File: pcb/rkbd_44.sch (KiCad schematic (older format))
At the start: 16 parts, among them SW1 SW_Push, U1 ATmega32U4-AU, Y1 16MHz

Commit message: pcb new
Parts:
- R1, R2, R3, R4: footprint Keebio-Parts:R_0805 -> Resistor_SMD:R_0805_2012Metric
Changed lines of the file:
@@
 F 0 "R4" V 4229 3390 50  0000 C CNN
 F 1 "10k" V 4320 3390 50  0000 C CNN
-F 2 "Keebio-Parts:R_0805" H 4425 3390 50  0001 C CNN
+F 2 "Resistor_SMD:R_0805_2012Metric" H 4425 3390 50  0001 C CNN
 F 3 "~" H 4425 3390 50  0001 C CNN
 	1    4425 3390
@@
 F 0 "R2" V 2299 2290 50  0000 C CNN
 F 1 "22" V 2390 2290 50  0000 C CNN
-F 2 "Keebio-Parts:R_0805" H 2495 2290 50  0001 C CNN
+F 2 "Resistor_SMD:R_0805_2012Metric" H 2495 2290 50  0001 C CNN
 F 3 "~" H 2495 2290 50  0001 C CNN
 	1    2495 2290
@@
 F 0 "R3" V 1994 2390 50  0000 C CNN
 F 1 "22" V 2085 2390 50  0000 C CNN
-F 2 "Keebio-Parts:R_0805" H 2190 2390 50  0001 C CNN
+F 2 "Resistor_SMD:R_0805_2012Metric" H 2190 2390 50  0001 C CNN
 F 3 "~" H 2190 2390 50  0001 C CNN
 	1    2190 2390
@@
 F 0 "R1" H 2686 1094 50  0000 R CNN
 F 1 "10k" H 2686 1185 50  0000 R CNN
-F 2 "Keebio-Parts:R_0805" H 2745 1140 50  0001 C CNN
+F 2 "Resistor_SMD:R_0805_2012Metric" H 2745 1140 50  0001 C CNN
 F 3 "~" H 2745 1140 50  0001 C CNN
 	1    2745 1140

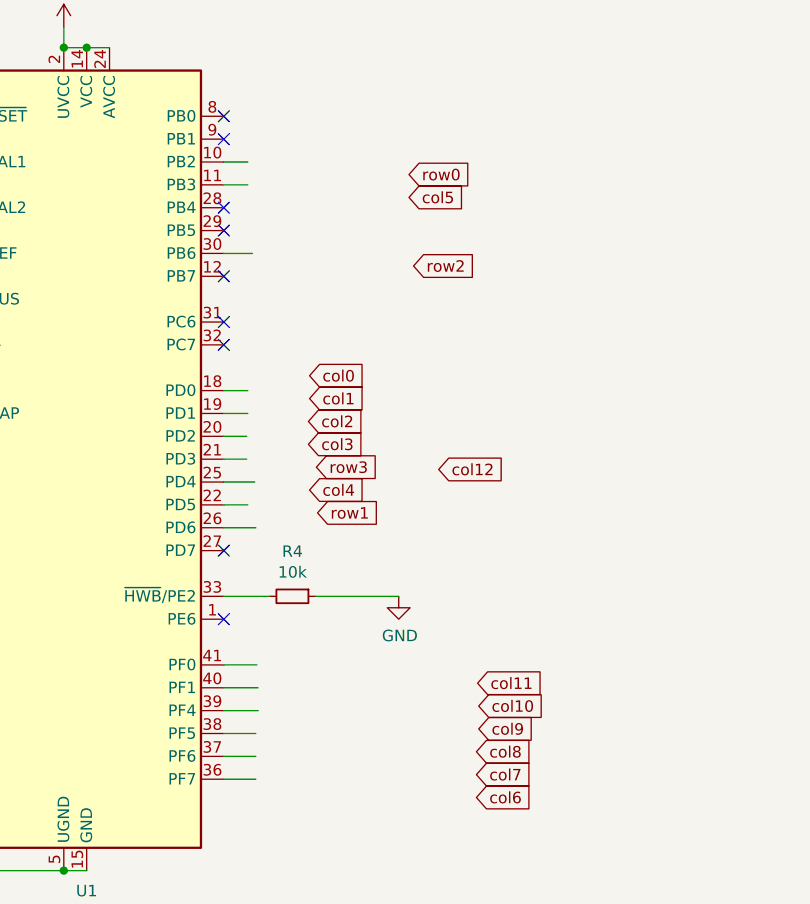
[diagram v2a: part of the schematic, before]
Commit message: add cutting line
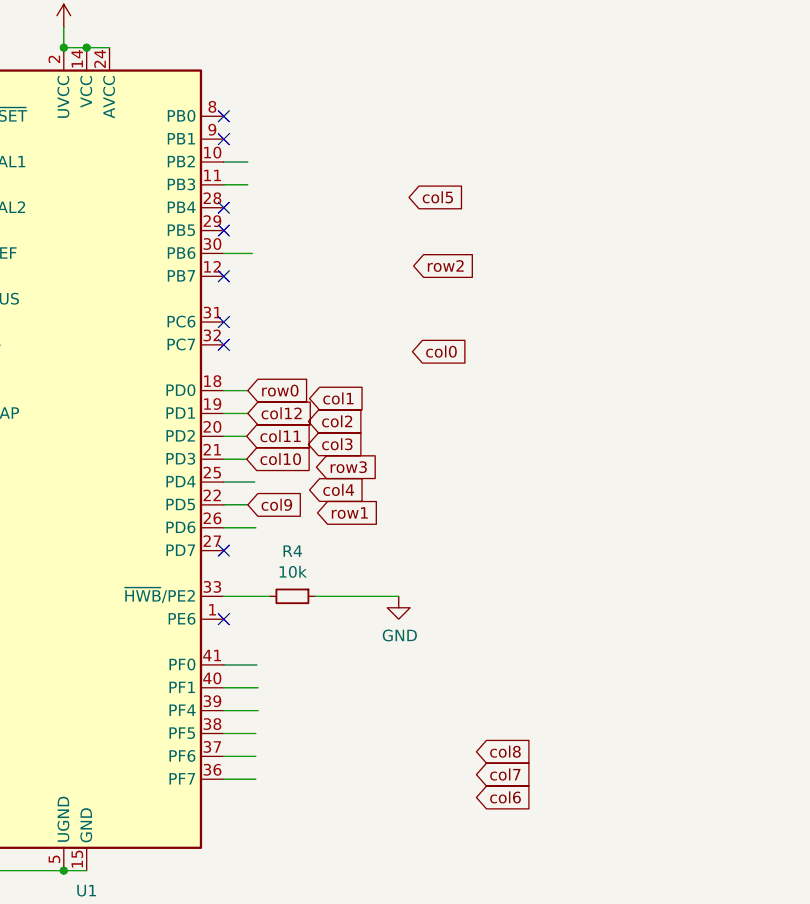
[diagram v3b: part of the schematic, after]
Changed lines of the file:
@@
 Text GLabel 5230 4070 2    50   Input ~ 0
 col8
-Text GLabel 5240 3970 2    50   Input ~ 0
+Text GLabel 4230 2990 2    50   Input ~ 0
 col9
-Text GLabel 5240 3870 2    50   Input ~ 0
+Text GLabel 4225 2790 2    50   Input ~ 0
 col10
 Text GLabel 4530 2825 2    50   Input ~ 0
@@
 Text GLabel 4955 1945 2    50   Input ~ 0
 row2
-Text GLabel 4935 1545 2    50   Input ~ 0
+Text GLabel 4230 2490 2    50   Input ~ 0
 row0
 Wire Wire Line
@@
 Wire Wire Line
 	4265 3090 4125 3090
-Text GLabel 5235 3770 2    50   Input ~ 0
+Text GLabel 4225 2690 2    50   Input ~ 0
 col11
 Text GLabel 4500 2525 2    50   Input ~ 0
 col1
-Text GLabel 4500 2425 2    50   Input ~ 0
+Text GLabel 4950 2320 2    50   Input ~ 0
 col0
 Text GLabel 4535 3025 2    50   Input ~ 0
@@
 Wire Wire Line
 	1970 1290 2060 1290
-Text GLabel 5065 2835 2    50   Input ~ 0
+Text GLabel 4230 2590 2    50   Input ~ 0
 col12
 Connection ~ 3425 4590

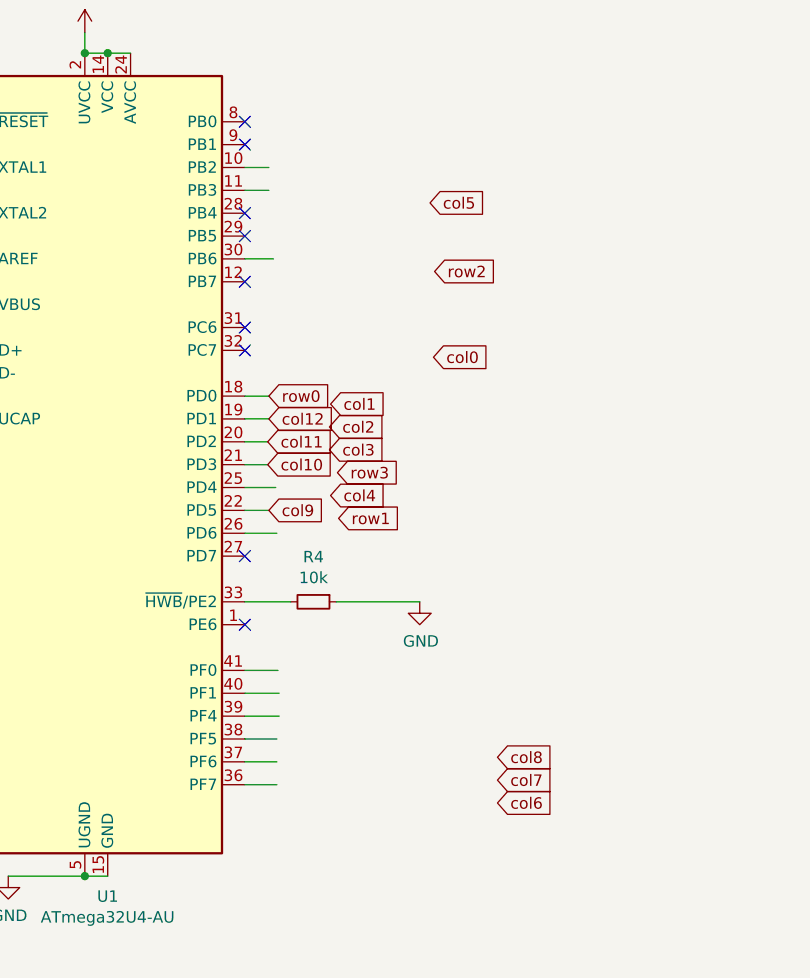
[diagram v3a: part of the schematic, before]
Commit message: Routing all, Ground fills
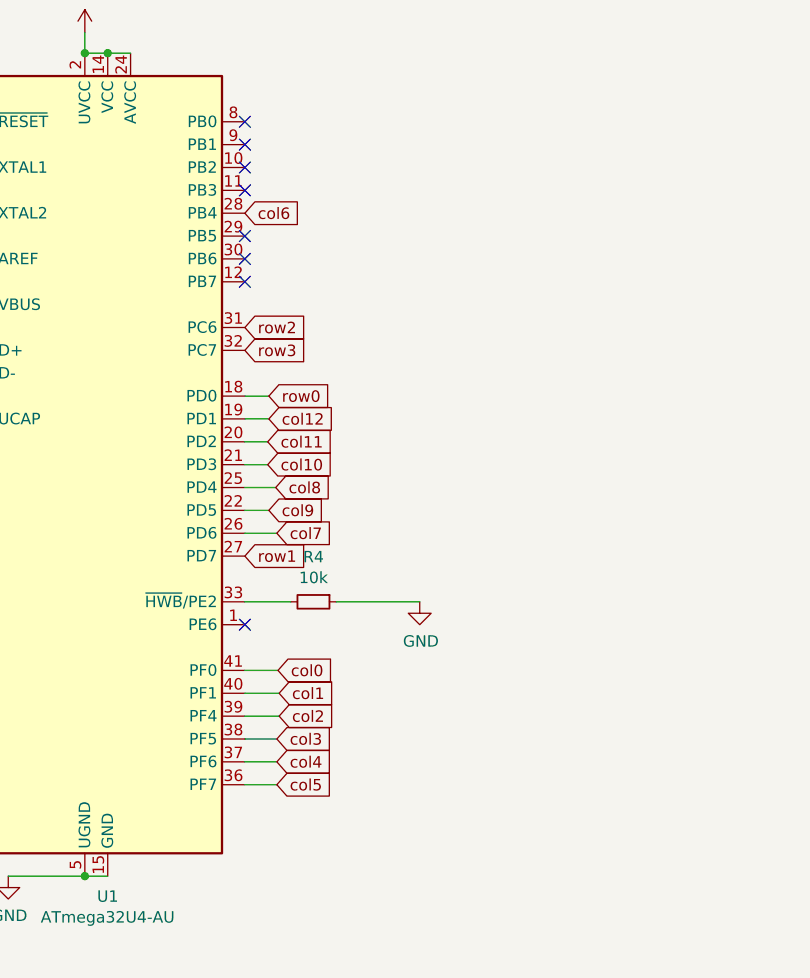
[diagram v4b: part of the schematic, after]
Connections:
- wire segments 69 -> 66
- no-connect marks 12 -> 11
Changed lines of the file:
@@
 F1 "matrix.sch" 50
 $EndSheet
-Text GLabel 4495 2725 2    50   Input ~ 0
+Text GLabel 4265 3990 2    50   Input ~ 0
 col3
-Text GLabel 4500 2925 2    50   Input ~ 0
+Text GLabel 4265 4090 2    50   Input ~ 0
 col4
-Text GLabel 4935 1645 2    50   Input ~ 0
+Text GLabel 4265 4190 2    50   Input ~ 0
 col5
-Text GLabel 5230 4270 2    50   Input ~ 0
+Text GLabel 4125 1690 2    50   Input ~ 0
 col6
-Text GLabel 5230 4170 2    50   Input ~ 0
+Text GLabel 4265 3090 2    50   Input ~ 0
 col7
-Text GLabel 5230 4070 2    50   Input ~ 0
+Text GLabel 4260 2890 2    50   Input ~ 0
 col8
 Text GLabel 4230 2990 2    50   Input ~ 0
@@
 Text GLabel 4225 2790 2    50   Input ~ 0
 col10
-Text GLabel 4530 2825 2    50   Input ~ 0
+Text GLabel 4125 2290 2    50   Input ~ 0
 row3
-Text GLabel 4955 1945 2    50   Input ~ 0
+Text GLabel 4125 2190 2    50   Input ~ 0
 row2
 Text GLabel 4230 2490 2    50   Input ~ 0
 row0
-Wire Wire Line
-	4125 1490 4230 1490
-Wire Wire Line
-	4125 1590 4230 1590
 Wire Wire Line
 	4265 4190 4125 4190
@@
 	4230 2490 4125 2490
 Wire Wire Line
-	4125 1890 4250 1890
-Wire Wire Line
 	4265 3090 4125 3090
 Text GLabel 4225 2690 2    50   Input ~ 0
 col11
-Text GLabel 4500 2525 2    50   Input ~ 0
-col1
-Text GLabel 4950 2320 2    50   Input ~ 0
-col0
-Text GLabel 4535 3025 2    50   Input ~ 0
+Text GLabel 4125 3190 2    50   Input ~ 0
 row1
-Text GLabel 4495 2625 2    50   Input ~ 0
+Text GLabel 4275 3890 2    50   Input ~ 0
 col2
 Wire Wire Line
@@
 NoConn ~ 2925 1890
 NoConn ~ 4125 1990
-NoConn ~ 4125 2190
-NoConn ~ 4125 1690
 NoConn ~ 4125 1790
-NoConn ~ 4125 2290
-NoConn ~ 4125 3190
 NoConn ~ 4125 3490
 NoConn ~ 1460 4405
@@
 $EndComp
 NoConn ~ 4125 1390
+Text GLabel 4270 3690 2    50   Input ~ 0
+col0
+Text GLabel 4275 3790 2    50   Input ~ 0
+col1
+NoConn ~ 4125 1490
+NoConn ~ 4125 1590
+NoConn ~ 4125 1890
 $EndSCHEMATC

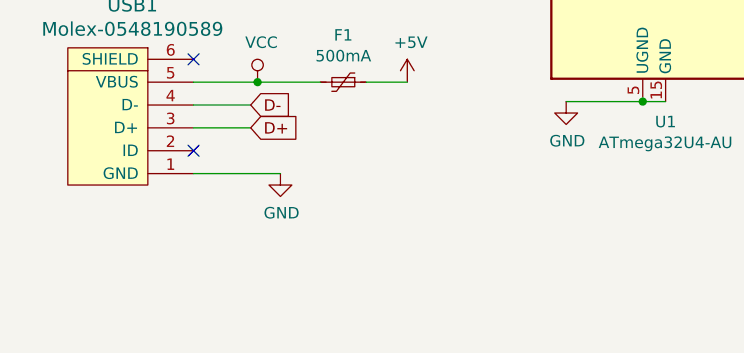
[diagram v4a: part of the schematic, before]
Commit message: Fill zones, fix drc erro
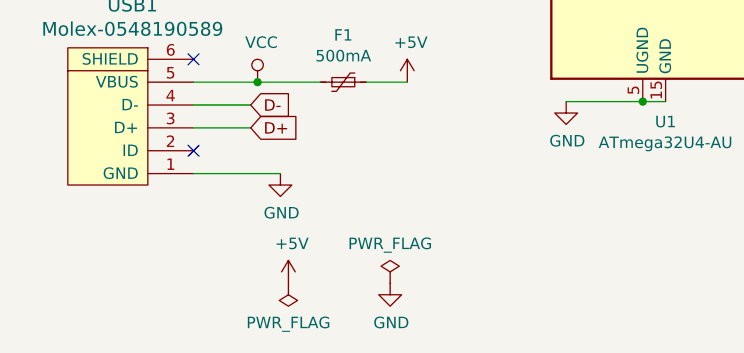
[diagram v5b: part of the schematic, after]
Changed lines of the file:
@@
 NoConn ~ 4125 1590
 NoConn ~ 4125 1890
+$Comp
+L power:PWR_FLAG #FLG0101
+U 1 1 5E3AE8CE
+P 2320 5385
+F 0 "#FLG0101" H 2320 5460 50  0001 C CNN
+F 1 "PWR_FLAG" H 2320 5558 50  0000 C CNN
+F 2 "" H 2320 5385 50  0001 C CNN
+F 3 "~" H 2320 5385 50  0001 C CNN
+	1    2320 5385
+	1    0    0    -1
+$EndComp
+$Comp
+L power:PWR_FLAG #FLG0102
+U 1 1 5E3AEF10
+P 1875 5385
+F 0 "#FLG0102" H 1875 5460 50  0001 C CNN
+F 1 "PWR_FLAG" H 1875 5558 50  0000 C CNN
+F 2 "" H 1875 5385 50  0001 C CNN
+F 3 "~" H 1875 5385 50  0001 C CNN
+	1    1875 5385
+	-1   0    0    1
+$EndComp
+$Comp
+L power:GND #PWR0114
+U 1 1 5E3B2097
+P 2320 5385
+F 0 "#PWR0114" H 2320 5135 50  0001 C CNN
+F 1 "GND" H 2325 5212 50  0000 C CNN
+F 2 "" H 2320 5385 50  0001 C CNN
+F 3 "" H 2320 5385 50  0001 C CNN
+	1    2320 5385
+	1    0    0    -1
+$EndComp
+$Comp
+L power:+5V #PWR0115
+U 1 1 5E3B2645
+P 1875 5385
+F 0 "#PWR0115" H 1875 5235 50  0001 C CNN
+F 1 "+5V" H 1890 5558 50  0000 C CNN
+F 2 "" H 1875 5385 50  0001 C CNN
+F 3 "" H 1875 5385 50  0001 C CNN
+	1    1875 5385
+	1    0    0    -1
+$EndComp
 $EndSCHEMATC

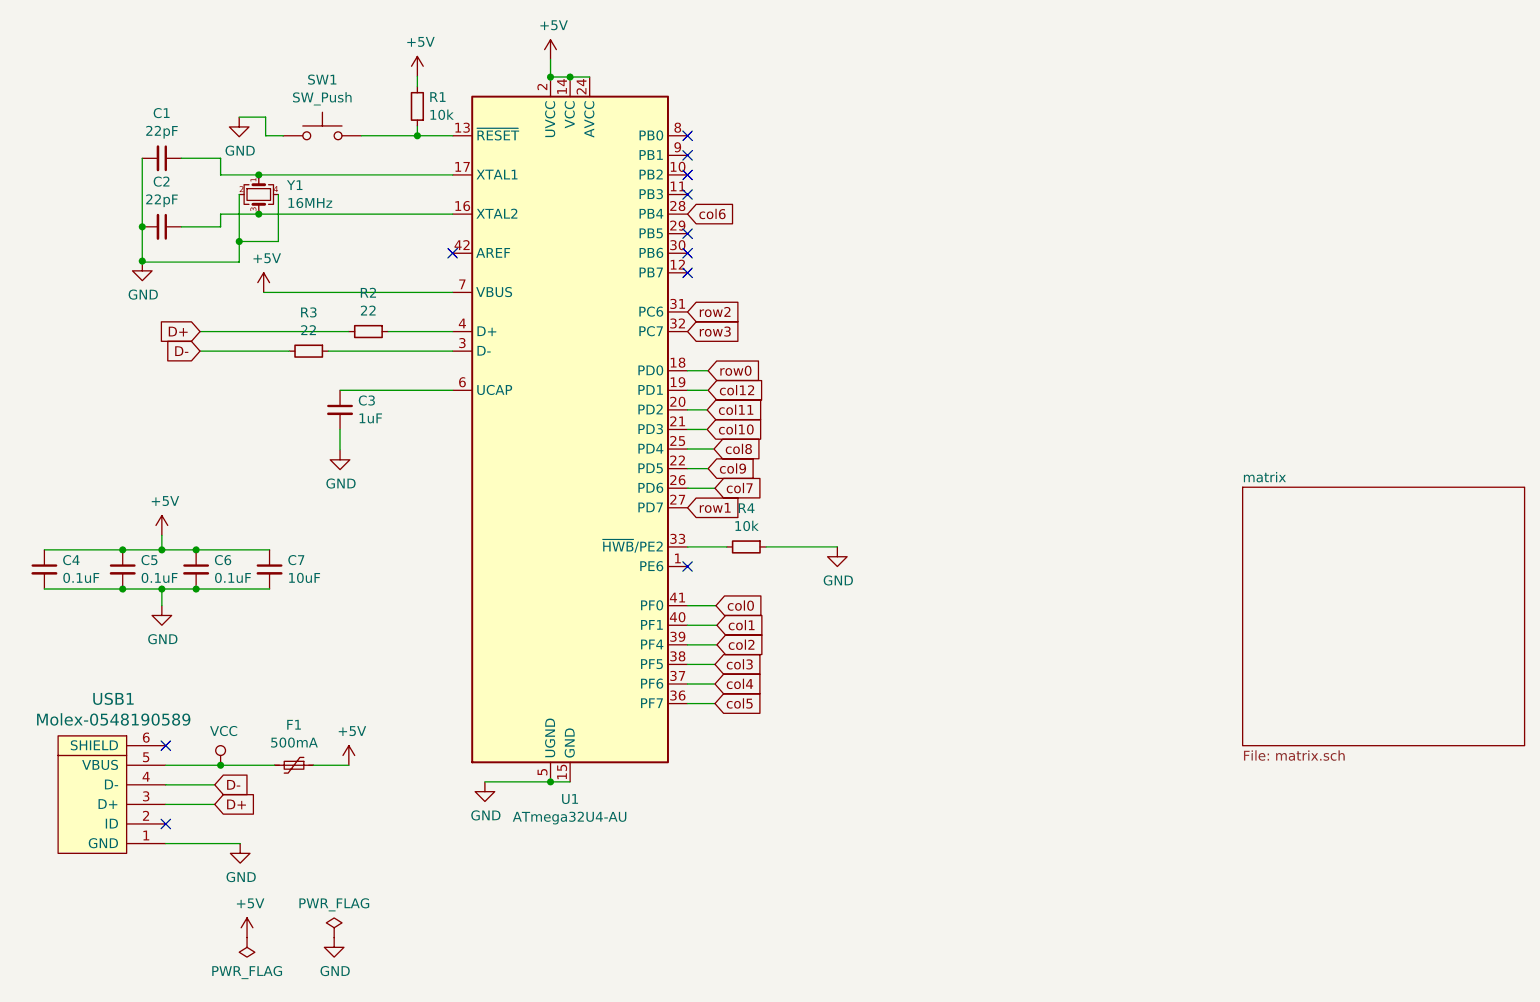
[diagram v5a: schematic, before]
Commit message: mcu change promicro
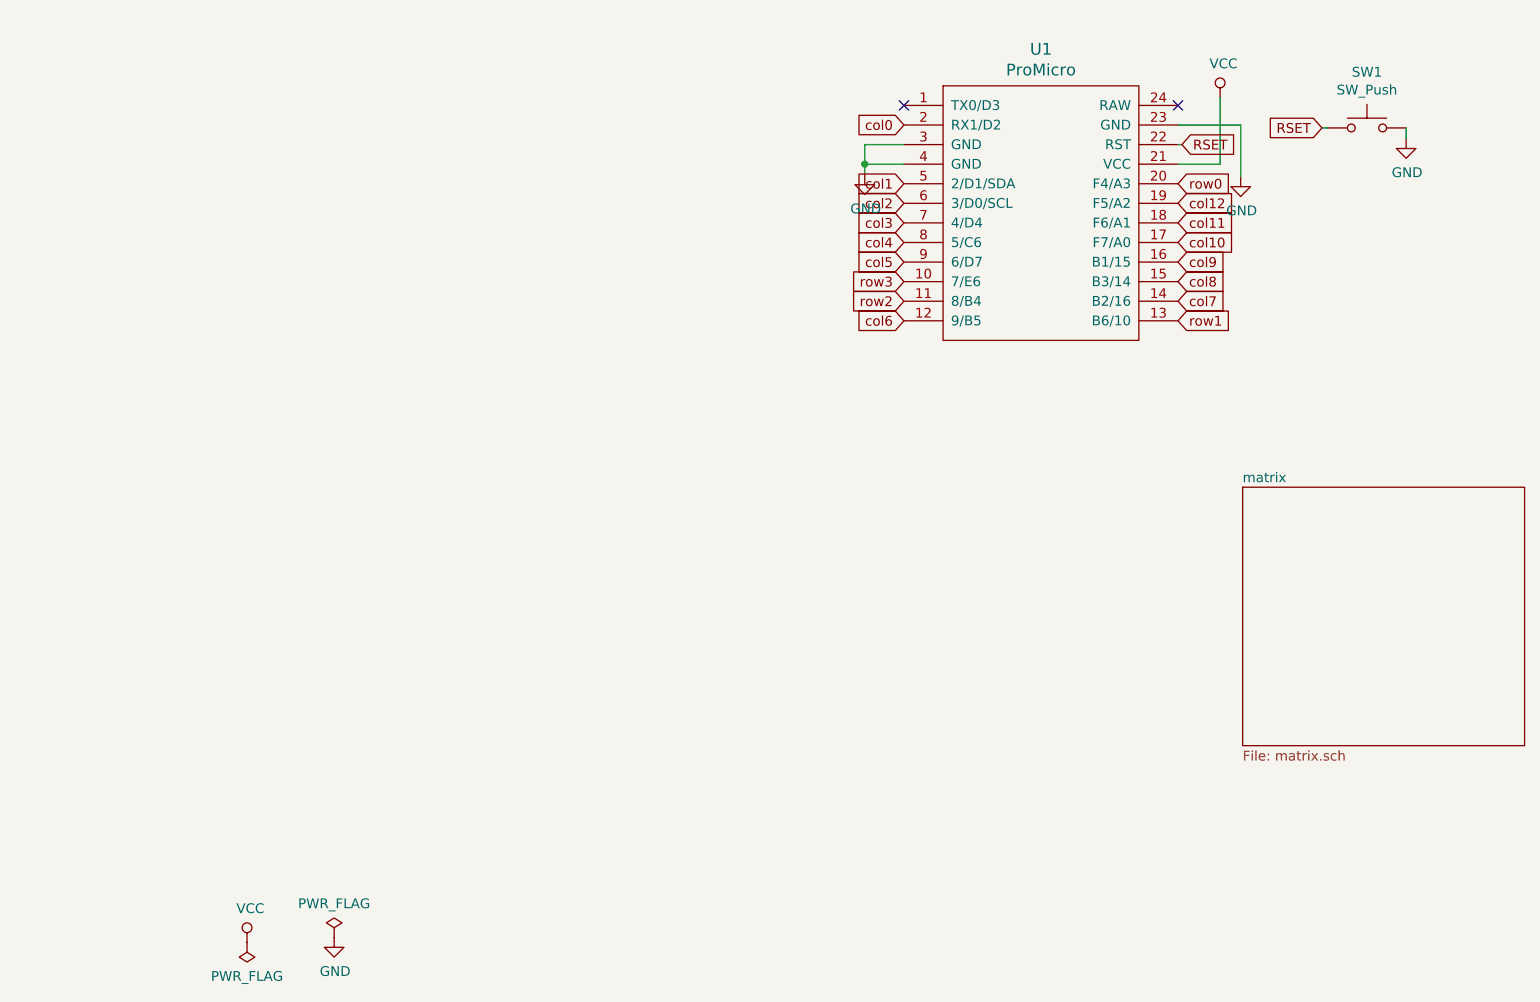
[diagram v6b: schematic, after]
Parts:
- removed C1, C2: 22pF, Capacitor_SMD:C_0805_2012Metric_Pad1.15x1.40mm_HandSolder, symbol Device:C_Small
- removed C3: 1uF, Capacitor_SMD:C_0805_2012Metric_Pad1.15x1.40mm_HandSolder, symbol Device:C_Small
- removed C4, C5, C6: 0.1uF, Capacitor_SMD:C_0805_2012Metric_Pad1.15x1.40mm_HandSolder, symbol Device:C_Small
- removed C7: 10uF, Capacitor_SMD:C_0805_2012Metric_Pad1.15x1.40mm_HandSolder, symbol Device:C_Small
- removed F1: 500mA, Fuse:Fuse_1206_3216Metric_Pad1.42x1.75mm_HandSolder, symbol Device:Polyfuse_Small
- removed R1, R4: 10k, Resistor_SMD:R_0805_2012Metric, symbol Device:R_Small
- removed R2, R3: 22, Resistor_SMD:R_0805_2012Metric, symbol Device:R_Small
- removed U1: ATmega32U4-AU, Package_QFP:TQFP-44_10x10mm_P0.8mm, symbol MCU_Microchip_ATmega:ATmega32U4-AU
- removed USB1: Molex-0548190589, random-keyboard-parts:Molex-0548190589, symbol random-keyboard-parts:Molex-0548190589
- removed Y1: 16MHz, Crystal:Crystal_SMD_3225-4Pin_3.2x2.5mm_HandSoldering, symbol Device:Crystal_GND24_Small
- added U1: ProMicro, kbd:ProMicro_v3.5, symbol kbd:ProMicro
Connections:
- net GND: now also SW1.2, U1.23 (GND), U1.3 (GND), U1.4 (GND); no longer SW1.1
- net VCC: now also U1.21 (VCC)
- net col0: now also U1.2 (RX1/D2)
- net col1: now also U1.5 (2/D1/SDA)
- net col10: now also U1.17 (F7/A0)
- net col11: now also U1.18 (F6/A1)
- net col12: now also U1.19 (F5/A2)
- net col2: now also U1.6 (3/D0/SCL)
- net col3: now also U1.7 (4/D4)
- net col4: now also U1.8 (5/C6)
- net col5: now also U1.9 (6/D7)
- net col6: now also U1.12 (9/B5)
- net col7: now also U1.14 (B2/16)
- net col8: now also U1.15 (B3/14)
- net col9: now also U1.16 (B1/15)
- net row0: now also U1.20 (F4/A3)
- net row1: now also U1.13 (B6/10)
- net row2: now also U1.11 (8/B4)
- net row3: now also U1.10 (7/E6)
- new net RSET: SW1.1, U1.22 (RST)
- no-connect marks 11 -> 2
